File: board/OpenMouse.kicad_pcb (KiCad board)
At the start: 2 copper layers, 40 parts, among them Q1 BSS138, Q2 BSS138, Q3 BSS138, Q4 BSS138, Q5 BSS138, SW1 MB1, SW2 MB2, SW3 MB3, T1 Teensy_2.0, U1 PMW3389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

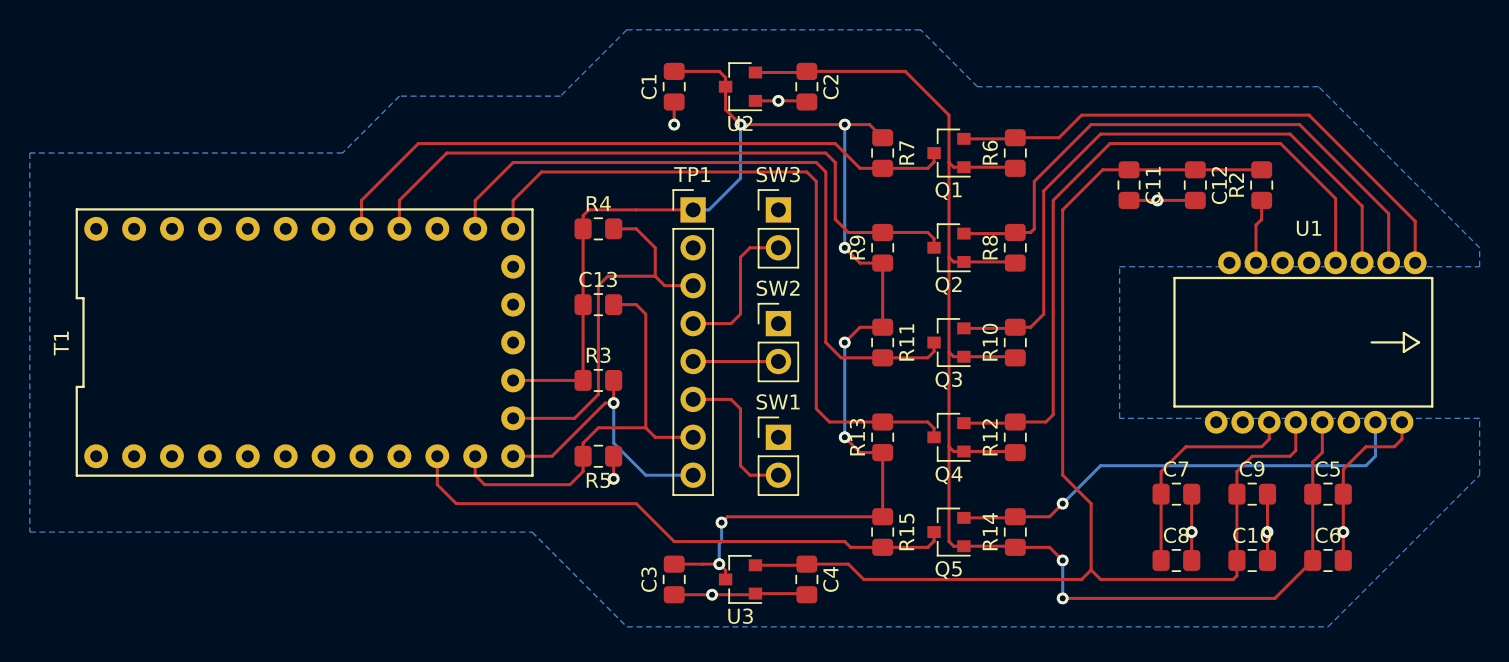
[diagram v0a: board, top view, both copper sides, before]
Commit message: Reroute 5V line to reduce vias
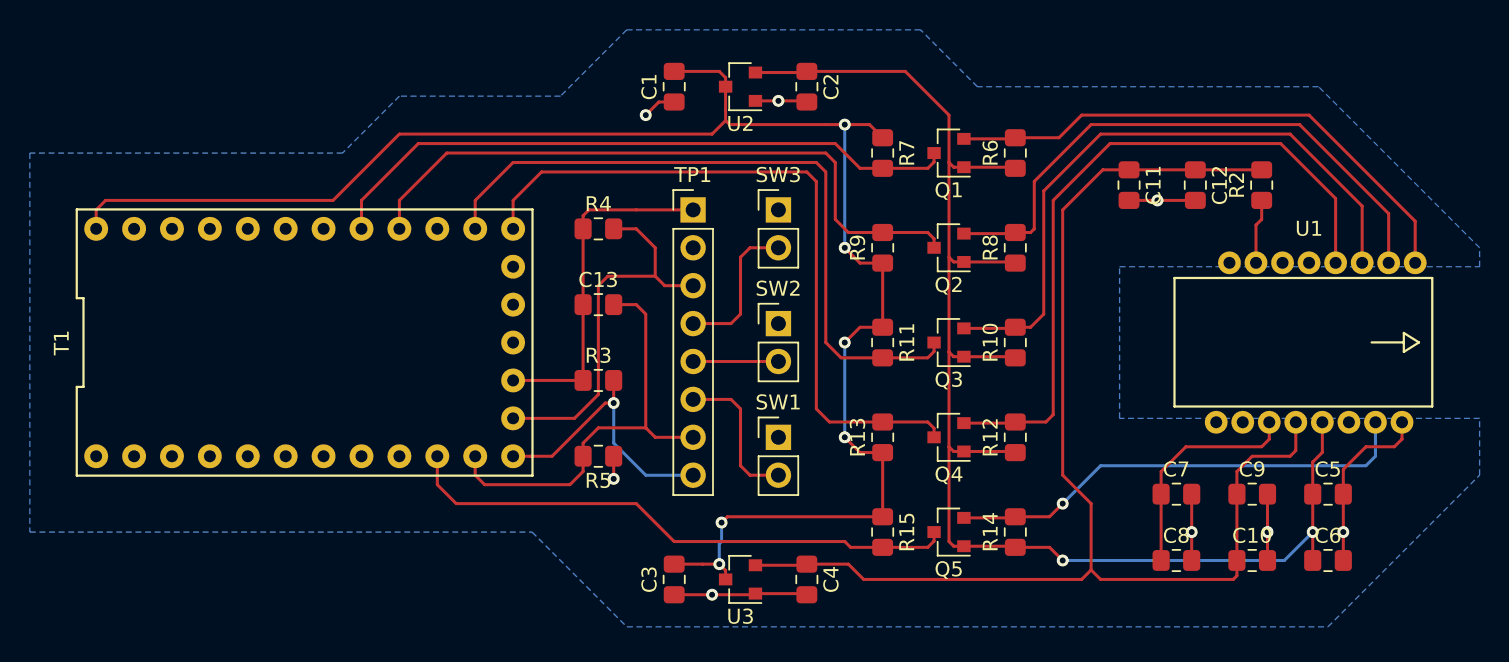
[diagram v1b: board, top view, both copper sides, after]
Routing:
- net +5V: track 98.1 -> 136.8 mm, vias 7 -> 6
- net +3V3: track 99.2 -> 96.4 mm
- net GND: track 40.8 -> 41.6 mm
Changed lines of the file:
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@@
   (layers
     (0 F.Cu signal)
-    (31 B.Cu signal hide)
+    (31 B.Cu signal)
     (32 B.Adhes user)
     (33 F.Adhes user)
@@
   (segment (start 125.02 70.8) (end 125.095 70.875) (width 0.2032) (layer F.Cu) (net 2))
   (segment (start 121.65 70.8) (end 125.02 70.8) (width 0.2032) (layer F.Cu) (net 2))
-  (segment (start 145.025 97.155) (end 145.025 92.71) (width 0.2032) (layer F.Cu) (net 2))
+  (segment (start 145.025 97.155) (end 145.025 95.25) (width 0.2032) (layer F.Cu) (net 2))
   (segment (start 111.05 64.455) (end 111.125 64.38) (width 0.2032) (layer F.Cu) (net 2))
   (segment (start 107.68 64.455) (end 111.05 64.455) (width 0.2032) (layer F.Cu) (net 2))
@@
   (segment (start 125.095 96.275) (end 127.39 96.275) (width 0.2032) (layer F.Cu) (net 2))
   (segment (start 127.39 96.275) (end 128.27 97.155) (width 0.2032) (layer F.Cu) (net 2))
-  (segment (start 145.025 97.155) (end 142.485 99.695) (width 0.2032) (layer F.Cu) (net 2))
-  (segment (start 142.485 99.695) (end 128.27 99.695) (width 0.2032) (layer F.Cu) (net 2))
-  (segment (start 128.27 99.695) (end 128.27 99.695) (width 0.2032) (layer F.Cu) (net 2))
-  (via (at 128.27 99.695) (size 0.8) (drill 0.4) (layers F.Cu B.Cu) (net 2))
   (segment (start 128.27 97.155) (end 128.27 97.155) (width 0.2032) (layer F.Cu) (net 2))
   (via (at 128.27 97.155) (size 0.8) (drill 0.4) (layers F.Cu B.Cu) (net 2))
-  (segment (start 128.27 97.155) (end 128.27 99.695) (width 0.2032) (layer B.Cu) (net 2))
   (segment (start 145.025 92.71) (end 145.025 90.56) (width 0.2032) (layer F.Cu) (net 2))
   (segment (start 145.67 89.915) (end 145.67 87.892) (width 0.2032) (layer F.Cu) (net 2))
   (segment (start 145.025 90.56) (end 145.67 89.915) (width 0.2032) (layer F.Cu) (net 2))
+  (segment (start 145.025 95.25) (end 145.025 92.71) (width 0.2032) (layer F.Cu) (net 2))
+  (via (at 145.025 95.25) (size 0.8) (drill 0.4) (layers F.Cu B.Cu) (net 2))
+  (segment (start 143.12 97.155) (end 145.025 95.25) (width 0.2032) (layer B.Cu) (net 2))
+  (segment (start 128.27 97.155) (end 143.12 97.155) (width 0.2032) (layer B.Cu) (net 2))
   (segment (start 119.65 75.5968) (end 119.65 76.2) (width 0.2032) (layer F.Cu) (net 3))
   (segment (start 119.2282 75.175) (end 119.65 75.5968) (width 0.2032) (layer F.Cu) (net 3))
@@
   (segment (start 104.14 97.4) (end 105.2582 97.4) (width 0.2032) (layer F.Cu) (net 4))
   (segment (start 115.325 67.945) (end 116.205 68.825) (width 0.2032) (layer F.Cu) (net 4))
-  (segment (start 106.68 67.945) (end 106.68 67.945) (width 0.2032) (layer F.Cu) (net 4))
   (segment (start 105.68 65.405) (end 105.68 66.945) (width 0.2032) (layer F.Cu) (net 4))
-  (segment (start 105.68 66.945) (end 106.68 67.945) (width 0.2032) (layer F.Cu) (net 4))
-  (segment (start 112.395 67.945) (end 113.665 67.945) (width 0.2032) (layer F.Cu) (net 4))
   (segment (start 116.205 94.225) (end 116.205 89.925) (width 0.2032) (layer F.Cu) (net 4))
   (segment (start 116.205 81.525) (end 116.205 77.225) (width 0.2032) (layer F.Cu) (net 4))
@@
   (segment (start 105.2582 96.0368) (end 105.2582 97.4) (width 0.2032) (layer B.Cu) (net 4))
   (segment (start 105.41 95.885) (end 105.2582 96.0368) (width 0.2032) (layer B.Cu) (net 4))
-  (segment (start 106.68 67.945) (end 112.395 67.945) (width 0.2032) (layer F.Cu) (net 4))
-  (via (at 106.68 67.945) (size 0.8) (drill 0.4) (layers F.Cu B.Cu) (net 4))
-  (segment (start 106.68 68.510685) (end 106.68 67.945) (width 0.2032) (layer B.Cu) (net 4))
-  (segment (start 106.68 71.5382) (end 106.68 68.510685) (width 0.2032) (layer B.Cu) (net 4))
-  (segment (start 104.5582 73.66) (end 106.68 71.5382) (width 0.2032) (layer B.Cu) (net 4))
-  (segment (start 103.505 73.66) (end 104.5582 73.66) (width 0.2032) (layer B.Cu) (net 4))
+  (segment (start 105.68 67.675) (end 104.775 68.58) (width 0.2032) (layer F.Cu) (net 4))
+  (segment (start 104.775 68.58) (end 83.82 68.58) (width 0.2032) (layer F.Cu) (net 4))
+  (segment (start 105.68 66.945) (end 105.68 67.675) (width 0.2032) (layer F.Cu) (net 4))
+  (segment (start 79.375 73.025) (end 64.135 73.025) (width 0.2032) (layer F.Cu) (net 4))
+  (segment (start 63.5 73.66) (end 63.5 74.93) (width 0.2032) (layer F.Cu) (net 4))
+  (segment (start 83.82 68.58) (end 79.375 73.025) (width 0.2032) (layer F.Cu) (net 4))
+  (segment (start 64.135 73.025) (end 63.5 73.66) (width 0.2032) (layer F.Cu) (net 4))
+  (segment (start 112.395 67.945) (end 113.665 67.945) (width 0.2032) (layer F.Cu) (net 4))
+  (segment (start 105.68 67.675) (end 105.95 67.945) (width 0.2032) (layer F.Cu) (net 4))
+  (segment (start 105.95 67.945) (end 112.395 67.945) (width 0.2032) (layer F.Cu) (net 4))
   (segment (start 119.65 95.8532) (end 119.65 95.25) (width 0.2032) (layer F.Cu) (net 5))
   (segment (start 119.2282 96.275) (end 119.65 95.8532) (width 0.2032) (layer F.Cu) (net 5))
@@
   (segment (start 107.68 66.355) (end 109.22 66.355) (width 0.2032) (layer F.Cu) (net 13))
   (segment (start 132.715 73.025) (end 134.62 73.025) (width 0.2032) (layer F.Cu) (net 13))
-  (segment (start 98.18 90.17) (end 98.18 91.685) (width 0.2032) (layer F.Cu) (net 13))
-  (segment (start 98.18 91.685) (end 98.18 91.685) (width 0.2032) (layer F.Cu) (net 13))
-  (via (at 98.18 91.685) (size 0.8) (drill 0.4) (layers F.Cu B.Cu) (net 13))
   (segment (start 104.775 99.45) (end 107.605 99.45) (width 0.2032) (layer F.Cu) (net 13))
   (via (at 104.775 99.45) (size 0.8) (drill 0.4) (layers F.Cu B.Cu) (net 13))
@@
   (segment (start 109.22 66.355) (end 111.05 66.355) (width 0.2032) (layer F.Cu) (net 13))
   (via (at 109.22 66.355) (size 0.8) (drill 0.4) (layers F.Cu B.Cu) (net 13))
-  (segment (start 102.235 66.43) (end 102.235 67.945) (width 0.2032) (layer F.Cu) (net 13))
-  (segment (start 102.235 67.945) (end 102.235 67.945) (width 0.2032) (layer F.Cu) (net 13))
-  (via (at 102.235 67.945) (size 0.8) (drill 0.4) (layers F.Cu B.Cu) (net 13))
+  (via (at 100.33 67.31) (size 0.8) (drill 0.4) (layers F.Cu B.Cu) (net 13))
+  (segment (start 98.18 91.685) (end 98.18 91.685) (width 0.2032) (layer F.Cu) (net 13))
+  (segment (start 98.18 90.17) (end 98.18 91.685) (width 0.2032) (layer F.Cu) (net 13))
+  (via (at 98.18 91.685) (size 0.8) (drill 0.4) (layers F.Cu B.Cu) (net 13))
+  (segment (start 101.21 66.43) (end 100.33 67.31) (width 0.2032) (layer F.Cu) (net 13))
+  (segment (start 102.235 66.43) (end 101.21 66.43) (width 0.2032) (layer F.Cu) (net 13))
   (segment (start 95.25 92.075) (end 96.13 91.195) (width 0.2032) (layer F.Cu) (net 14))
   (segment (start 96.13 91.195) (end 96.13 90.17) (width 0.2032) (layer F.Cu) (net 14))
@@
   (segment (start 98.18 86.605) (end 98.18 86.605) (width 0.2032) (layer F.Cu) (net 16))
   (via (at 98.18 86.605) (size 0.8) (drill 0.4) (layers F.Cu B.Cu) (net 16))
-  (segment (start 103.505 91.44) (end 100.33 91.44) (width 0.2032) (layer B.Cu) (net 16))
-  (segment (start 98.18 89.29) (end 98.18 86.605) (width 0.2032) (layer B.Cu) (net 16))
-  (segment (start 100.33 91.44) (end 98.18 89.29) (width 0.2032) (layer B.Cu) (net 16))
   (segment (start 94.049315 90.17) (end 92.57137 90.17) (width 0.2032) (layer F.Cu) (net 16))
   (segment (start 92.57137 90.17) (end 91.44 90.17) (width 0.2032) (layer F.Cu) (net 16))
   (segment (start 98.18 86.605) (end 97.614315 86.605) (width 0.2032) (layer F.Cu) (net 16))
   (segment (start 97.614315 86.605) (end 94.049315 90.17) (width 0.2032) (layer F.Cu) (net 16))
+  (segment (start 98.18 89.29) (end 98.18 86.605) (width 0.2032) (layer B.Cu) (net 16))
+  (segment (start 103.505 91.44) (end 100.33 91.44) (width 0.2032) (layer B.Cu) (net 16))
+  (segment (start 100.33 91.44) (end 98.18 89.29) (width 0.2032) (layer B.Cu) (net 16))
   (segment (start 111.05 97.475) (end 111.125 97.4) (width 0.2032) (layer F.Cu) (net 17))
   (segment (start 107.68 97.475) (end 111.05 97.475) (width 0.2032) (layer F.Cu) (net 17))
